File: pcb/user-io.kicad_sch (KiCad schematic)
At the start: 26 parts, among them J4 FH12-16S-0.5SH(55), Q4 DMP3099L-7, Q6 DMG3418L, SW2 PEC12R-4222F-S0024, U150 SN74LVC1G14DBVR

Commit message: 1st step OEPSPN & MPN on components
- still missing new codes to be emitted
- project/schematic/components not tunned with Jon's project at this date
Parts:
- C293, C294: value 0.1uF -> 100nF; MPN (none) -> C1005X7R1E104K050BB; OEPSPN (none) -> OEPS010050
- C296, C303: MPN (none) -> GRM155R71E103KA01D; OEPSPN (none) -> OEPS010067
- C300, C302, C304, C305, C308: MPN (none) -> CL10A105KA8NNNC; OEPSPN (none) -> OEPS010022; Voltage 16V -> 25V
- C301, C306, C309: MPN (none) -> CL31B475KOHNNNE; OEPSPN (none) -> OEPS010081
- J4: MPN (none) -> FH12-16S-0.5SH(55); OEPSPN (none) -> espera
- Q4: MPN (none) -> DMP3099L-7; OEPSPN (none) -> espera
- Q6: MPN (none) -> DMG3418L; OEPSPN (none) -> espera
- R269, R279, R280, R281, R282: MPN (none) -> CRCW040210K0FKED; OEPSPN (none) -> OEPS020030
- R277: MPN (none) -> RC0402FR-13680KL; OEPSPN (none) -> OEPS020176
- R278: MPN (none) -> CRCW04021K00FKED; OEPSPN (none) -> OEPS020027
- R286, R287: MPN (none) -> ERJ-2RKF4702X; OEPSPN (none) -> OEPS020017
- SW2: MPN (none) -> PEC12R-4222F-S0024; OEPSPN (none) -> espera
- U150: MPN (none) -> SN74LVC1G14DBVR; OEPSPN (none) -> espera

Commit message: all OEPSPN
- all components with OEPSPN completed
- this Project Fork version not tunned with Project Main Branch
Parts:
- J4: OEPSPN espera -> OEPS070104
- Q4: OEPSPN espera -> OEPS060020
- Q6: MPN DMG3418L -> DMG3418L-7; OEPSPN espera -> OEPS060019
- SW2: OEPSPN espera -> OEPS070113
- U150: OEPSPN espera -> OEPS080160
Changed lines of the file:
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@@
 			)
 		)
-		(property "OEPSPN" "espera"
+		(property "OEPSPN" "OEPS060019"
 			(at 82.55 63.5 0)
 			(effects
@@
 			)
 		)
-		(property "MPN" "DMG3418L"
+		(property "MPN" "DMG3418L-7"
 			(at 82.55 63.5 0)
 			(effects
@@
 			)
 		)
-		(property "OEPSPN" "espera"
+		(property "OEPSPN" "OEPS080160"
 			(at 194.31 130.81 0)
 			(effects
@@
 			)
 		)
-		(property "OEPSPN" "espera"
+		(property "OEPSPN" "OEPS060020"
 			(at 97.79 54.61 0)
 			(effects
@@
 			)
 		)
-		(property "OEPSPN" "espera"
+		(property "OEPSPN" "OEPS070104"
 			(at 193.04 55.88 0)
 			(effects
@@
 			)
 		)
-		(property "OEPSPN" "espera"
+		(property "OEPSPN" "OEPS070113"
 			(at 139.7 133.35 0)
 			(effects

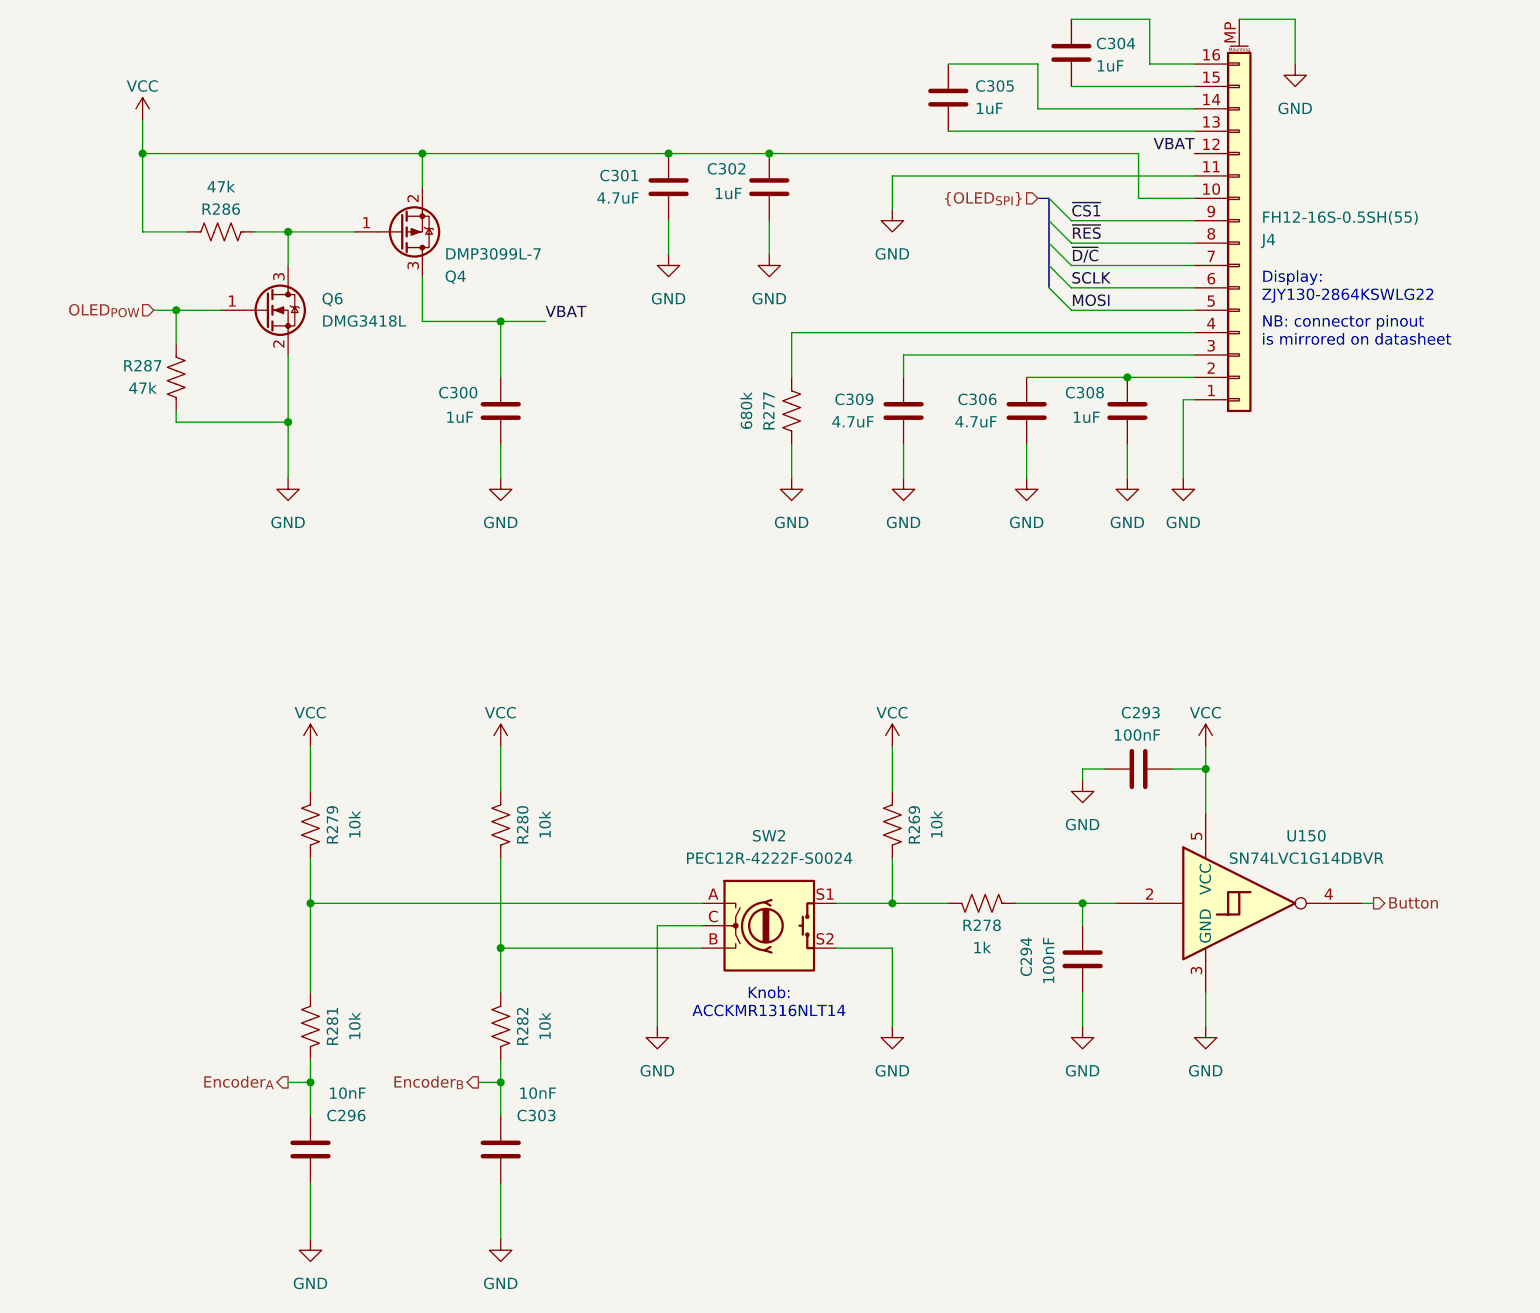
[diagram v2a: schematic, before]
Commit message: tunned with Main branch
- OEPSPN & MPN already on components
- missing 4 these codes
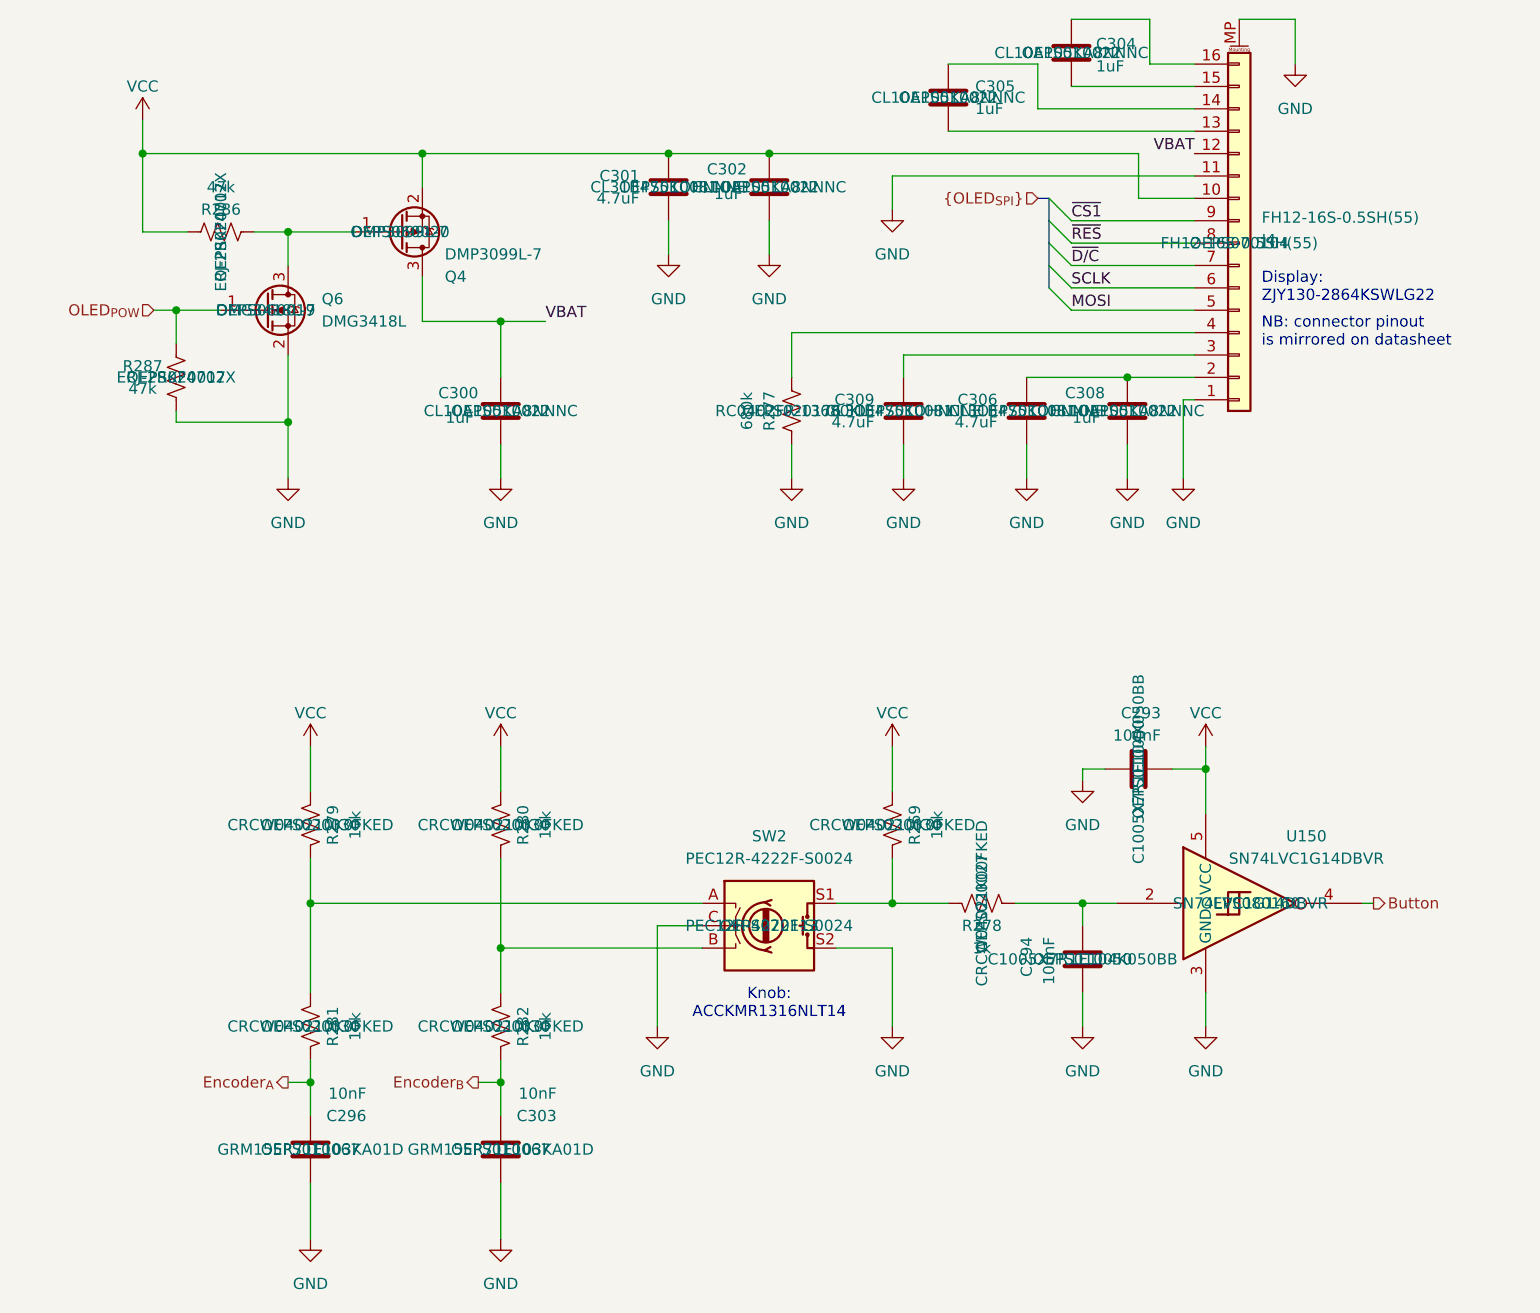
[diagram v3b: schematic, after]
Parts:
- C300, C302, C304, C305, C308: Voltage 25V -> 16V
